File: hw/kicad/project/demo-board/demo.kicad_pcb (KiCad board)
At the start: 2 copper layers, 49.5 x 49.5 mm, 28 parts, among them J2 MICRO_SD_HINGE, P1 ESP_CONN, P2 ESP_CONN, P3 ESP_CONN, P4 PWR_CONN, P5 CONN_DISPLAY, P6 SD_LCD_CONN, SW1 KEY_FLASH, SW2 KEY_RST, U1 NCP1117ST33T3G, U2 ESP-12E

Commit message: Silkscreen reviewed
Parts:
- JP1: value Jumper_NO_Small -> Jumper_Small
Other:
- board text added: "Made by Max Payne"
- board text added: "REV. A"

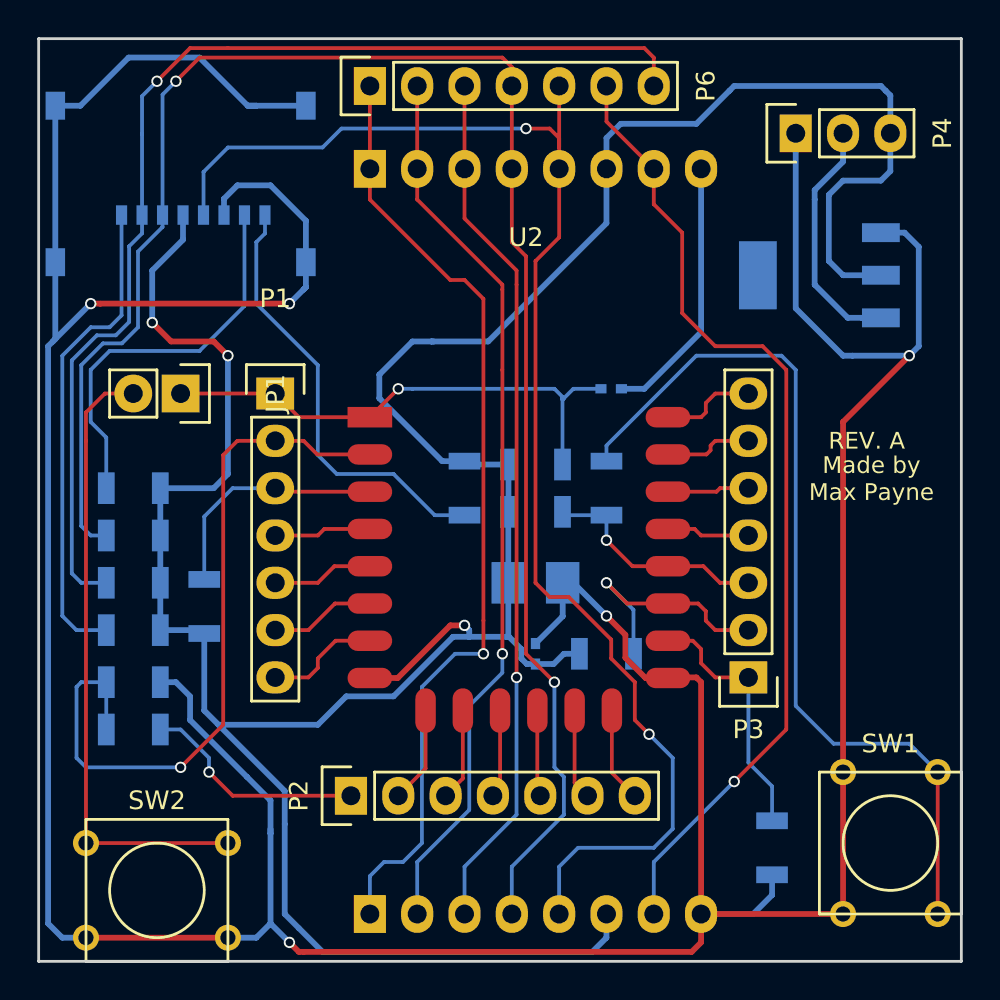
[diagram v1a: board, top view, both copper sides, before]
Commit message: Some connections and silkds clarified
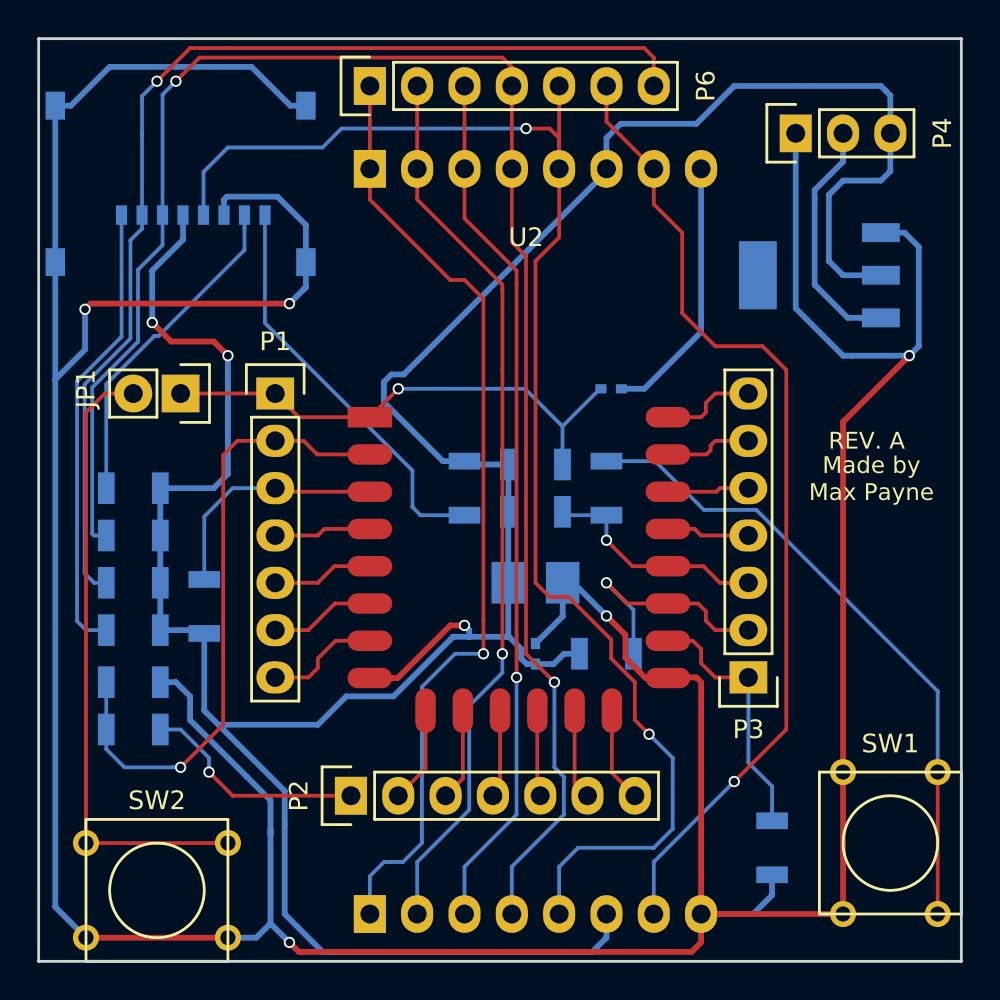
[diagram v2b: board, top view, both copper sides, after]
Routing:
- net Net-(R1-Pad2): track 48.1 -> 34.9 mm
- net /ADC: track 40.1 -> 34.2 mm
- net /SD_LCD_MISO: track 21.3 -> 17.9 mm
- net VCC: track 168.0 -> 165.7 mm
- net Net-(J2-Pad8): track 23.7 -> 21.9 mm
- net /SD_CS: track 60.1 -> 58.5 mm
- net Net-(J2-Pad1): track 26.1 -> 24.6 mm
- net /SD_LCD_MOSI: track 94.7 -> 93.9 mm
- net GND: track 250.7 -> 250.1 mm
- net /nRST: track 28.0 -> 27.4 mm

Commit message: Logo added
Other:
- board text added: "Demo Board REV. A"
- board text added: "F"
- board text added: "GO"
- board text added: "forgge @gmail.com"
- board text removed: "REV. A"
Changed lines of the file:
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@@
     (area 123.114999 69.774999 172.795001 119.455001)
     (thickness 1.6)
-    (drawings 6)
+    (drawings 13)
     (tracks 409)
     (zones 0)
@@
     (zone_45_only no)
     (trace_min 0.2032)
-    (segment_width 0.2)
-    (edge_width 0.15)
+    (segment_width 0.16)
+    (edge_width 0.16)
     (via_size 0.61)
     (via_drill 0.41)
@@
     (pcb_text_width 0.3)
     (pcb_text_size 1.5 1.5)
-    (mod_edge_width 0.15)
-    (mod_text_size 1 1)
-    (mod_text_width 0.15)
+    (mod_edge_width 0.16)
+    (mod_text_size 0.81 0.81)
+    (mod_text_width 0.16)
     (pad_size 1.524 1.524)
     (pad_drill 0.762)
@@
     (attr smd)
     (fp_text reference C1 (at -3.81 0) (layer B.SilkS)
-      (effects (font (size 1 1) (thickness 0.15)) (justify mirror))
+      (effects (font (size 1 1) (thickness 0.16)) (justify mirror))
     )
     (fp_text value 100uF (at -5.08 0.508) (layer B.Fab)
@@
     (tags "capacitor 0402")
     (attr smd)
-    (fp_text reference C3 (at 1.016 -1.524 360) (layer B.SilkS)
-      (effects (font (size 1 1) (thickness 0.15)) (justify mirror))
+    (fp_text reference C3 (at 1.016 -1.524 180) (layer B.SilkS)
+      (effects (font (size 1 1) (thickness 0.16)) (justify mirror))
     )
     (fp_text value 1nF (at 0 -3.048 90) (layer B.Fab)
@@
     (tags "pin header")
     (fp_text reference P3 (at 0 -2.794 180) (layer F.SilkS)
-      (effects (font (size 1 1) (thickness 0.15)))
+      (effects (font (size 1 1) (thickness 0.16)))
     )
     (fp_text value ESP_CONN (at 0 -4.318 180) (layer F.Fab)
@@
     (attr smd)
     (fp_text reference R1 (at 0 2.032 90) (layer B.SilkS)
-      (effects (font (size 1 1) (thickness 0.15)) (justify mirror))
+      (effects (font (size 1 1) (thickness 0.16)) (justify mirror))
     )
     (fp_text value 470 (at 3.048 0.254 180) (layer B.Fab)
@@
     (attr smd)
     (fp_text reference R2 (at -3.302 0) (layer B.SilkS)
-      (effects (font (size 1 1) (thickness 0.15)) (justify mirror))
+      (effects (font (size 1 1) (thickness 0.16)) (justify mirror))
     )
     (fp_text value 220k (at 4.318 0) (layer B.Fab)
@@
     (attr smd)
     (fp_text reference R3 (at 3.302 0 180) (layer B.SilkS)
-      (effects (font (size 1 1) (thickness 0.15)) (justify mirror))
+      (effects (font (size 1 1) (thickness 0.16)) (justify mirror))
     )
     (fp_text value 100k (at 0 0 180) (layer B.Fab) hide
@@
     (attr smd)
     (fp_text reference R7 (at 0 2.032) (layer B.SilkS)
-      (effects (font (size 1 1) (thickness 0.15)) (justify mirror))
+      (effects (font (size 1 1) (thickness 0.16)) (justify mirror))
     )
     (fp_text value 12k (at 0.254 -3.556) (layer B.Fab)
@@
     (attr smd)
     (fp_text reference R8 (at -3.302 0 90) (layer B.SilkS)
-      (effects (font (size 1 1) (thickness 0.15)) (justify mirror))
+      (effects (font (size 1 1) (thickness 0.16)) (justify mirror))
     )
     (fp_text value 12k (at 0 0 90) (layer B.Fab) hide
@@
     (attr smd)
     (fp_text reference R9 (at 0 -2.286) (layer B.SilkS)
-      (effects (font (size 1 1) (thickness 0.15)) (justify mirror))
+      (effects (font (size 1 1) (thickness 0.16)) (justify mirror))
     )
     (fp_text value 12k (at 0 0) (layer B.Fab) hide
@@
     (attr smd)
     (fp_text reference R10 (at 0 -2.286 90) (layer B.SilkS)
-      (effects (font (size 1 1) (thickness 0.15)) (justify mirror))
+      (effects (font (size 1 1) (thickness 0.16)) (justify mirror))
     )
     (fp_text value 12k (at 0 2.032 90) (layer B.Fab)
@@
     (attr smd)
     (fp_text reference R11 (at 0 2.3 270) (layer B.SilkS)
-      (effects (font (size 1 1) (thickness 0.15)) (justify mirror))
+      (effects (font (size 1 1) (thickness 0.16)) (justify mirror))
     )
     (fp_text value 50k (at 2.794 2.286 270) (layer B.Fab)
@@
     (attr smd)
     (fp_text reference R12 (at 3.81 0 180) (layer B.SilkS)
-      (effects (font (size 0.9 0.9) (thickness 0.15)) (justify mirror))
+      (effects (font (size 0.9 0.9) (thickness 0.16)) (justify mirror))
     )
     (fp_text value 50k (at -3.81 0 180) (layer B.Fab)
@@
     (attr smd)
     (fp_text reference R13 (at 3.81 0 180) (layer B.SilkS)
-      (effects (font (size 0.9 0.9) (thickness 0.15)) (justify mirror))
+      (effects (font (size 0.9 0.9) (thickness 0.16)) (justify mirror))
     )
     (fp_text value 50k (at -3.81 0 180) (layer B.Fab)
@@
     (attr smd)
     (fp_text reference R14 (at 3.81 0 180) (layer B.SilkS)
-      (effects (font (size 0.9 0.9) (thickness 0.15)) (justify mirror))
+      (effects (font (size 0.9 0.9) (thickness 0.16)) (justify mirror))
     )
     (fp_text value 50k (at 0.254 0 180) (layer B.Fab) hide
@@
     (attr smd)
     (fp_text reference R15 (at 3.81 0 180) (layer B.SilkS)
-      (effects (font (size 0.9 0.9) (thickness 0.15)) (justify mirror))
+      (effects (font (size 0.9 0.9) (thickness 0.16)) (justify mirror))
     )
     (fp_text value 50k (at 0 0 180) (layer B.Fab) hide
@@
     (at 168.91 113.03 270)
     (fp_text reference SW1 (at -5.334 0 360) (layer F.SilkS)
-      (effects (font (size 1 1) (thickness 0.15)))
+      (effects (font (size 1 1) (thickness 0.16)))
     )
     (fp_text value KEY_FLASH (at 0 -0.254 270) (layer F.Fab)
@@
     (at 129.54 115.57)
     (fp_text reference SW2 (at 0 -4.826) (layer F.SilkS)
-      (effects (font (size 1 1) (thickness 0.15)))
+      (effects (font (size 1 1) (thickness 0.16)))
     )
     (fp_text value KEY_RST (at 0 1.016) (layer F.Fab)
@@
     (tags "Module ESP-8266 ESP8266")
     (fp_text reference U2 (at 8.382 -9.652) (layer F.SilkS)
-      (effects (font (size 1 1) (thickness 0.15)))
+      (effects (font (size 1 1) (thickness 0.16)))
     )
     (fp_text value ESP-12E (at 8.128 -7.62) (layer F.Fab)
@@
     (tags "pin header")
     (fp_text reference P6 (at 0 18.034 90) (layer F.SilkS)
-      (effects (font (size 1 1) (thickness 0.15)))
+      (effects (font (size 1 1) (thickness 0.16)))
     )
     (fp_text value SD_LCD_CONN (at -1.778 7.366 180) (layer F.Fab)
@@
     )
   )
-  (gr_text "Made by \nMax Payne\n" (at 167.894 93.472) (layer F.SilkS)
-    (effects (font (size 0.9 0.9) (thickness 0.15)))
-  )
-  (gr_text "REV. A" (at 167.64 91.44) (layer F.SilkS)
-    (effects (font (size 0.9 0.9) (thickness 0.15)))
+  (gr_text "forgge\n@gmail.com" (at 167.894 101.854) (layer F.SilkS)
+    (effects (font (size 0.81 0.81) (thickness 0.15)))
+  )
+  (gr_arc (start 167.132 98.552) (end 167.894 98.552) (angle 90) (layer F.SilkS) (width 0.16))
+  (gr_arc (start 167.132 98.552) (end 168.148 98.552) (angle 90) (layer F.SilkS) (width 0.16))
+  (gr_arc (start 167.132 98.552) (end 167.64 98.552) (angle 90) (layer F.SilkS) (width 0.16))
+  (gr_text GO (at 170.18 98.806) (layer F.SilkS)
+    (effects (font (size 1.5 1.5) (thickness 0.3)))
+  )
+  (gr_text F (at 164.846 98.806) (layer F.SilkS)
+    (effects (font (size 1.5 1.5) (thickness 0.3)))
+  )
+  (gr_circle (center 167.132 98.552) (end 168.402 99.06) (layer F.SilkS) (width 0.2))
+  (gr_text "Made by \nMax Payne\n" (at 167.894 95.25) (layer F.SilkS)
+    (effects (font (size 0.9 0.9) (thickness 0.16)))
+  )
+  (gr_text "Demo Board\nREV. A" (at 167.894 92.202) (layer F.SilkS)
+    (effects (font (size 0.9 0.9) (thickness 0.16)))
   )
   (gr_line (start 172.72 119.38) (end 123.19 119.38) (angle 90) (layer Edge.Cuts) (width 0.15))

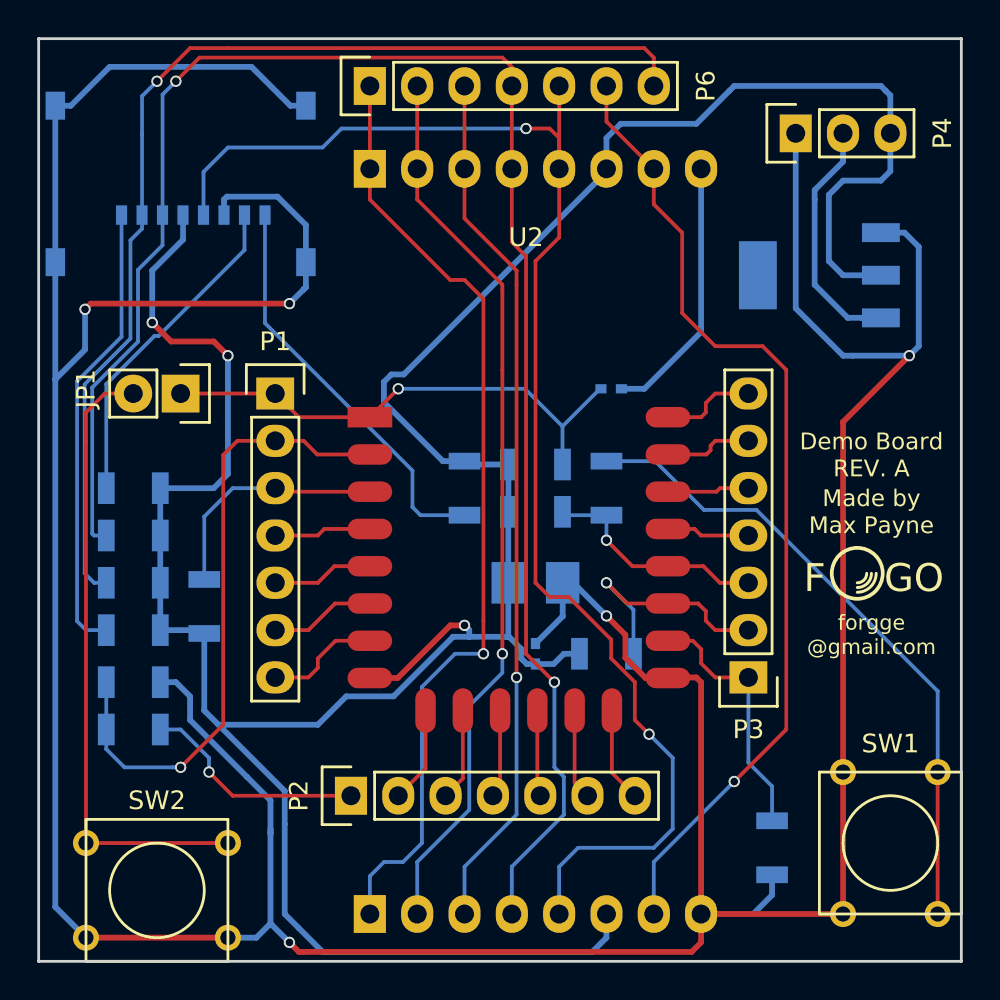
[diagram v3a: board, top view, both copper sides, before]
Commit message: Pushbuttons changed to the SMD type
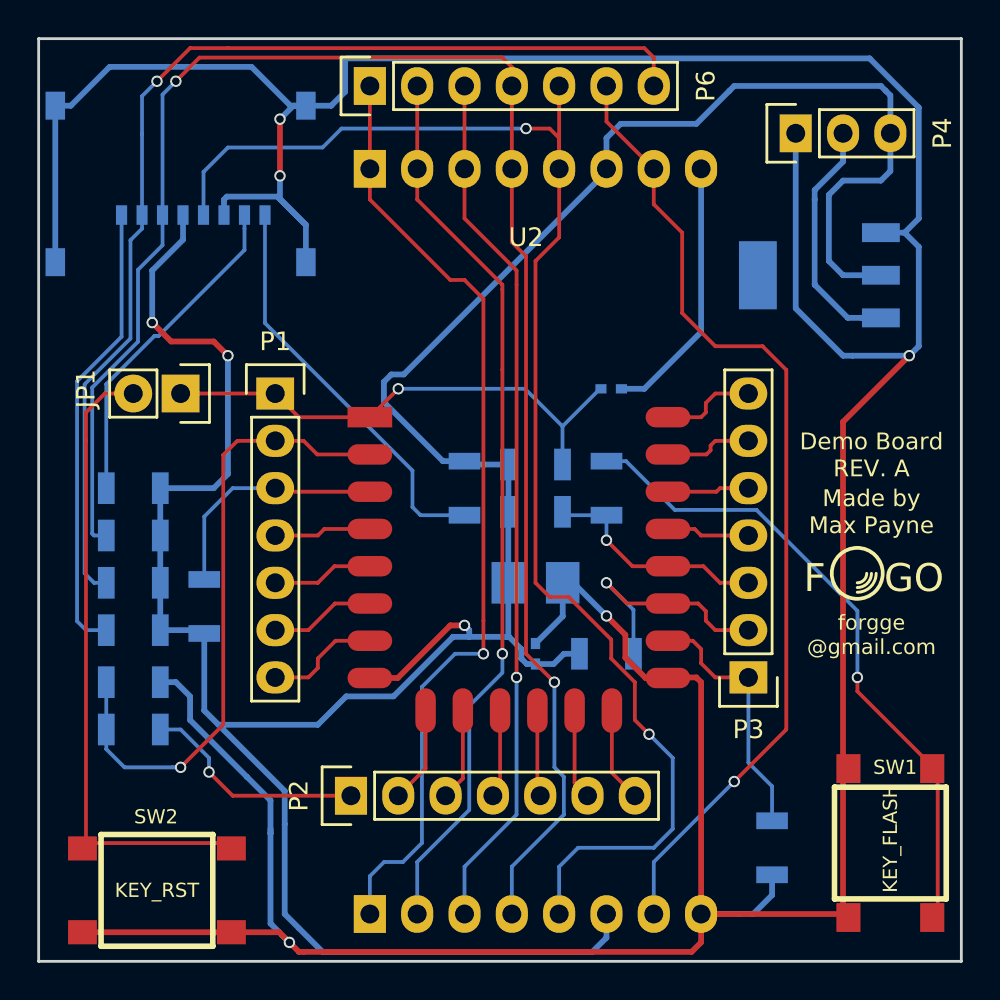
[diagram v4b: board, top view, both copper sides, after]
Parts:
- JP1: value Jumper_Small -> Jumper_NO_Small
- SW1, SW2: footprint Buttons_Switches_ThroughHole:SW_PUSH_SMALL -> kicadlib_local:SW_PUSH_SMD
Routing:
- net GND: track 250.1 -> 247.2 mm
- net Net-(R1-Pad2): track 34.9 -> 34.5 mm, vias 0 -> 1
